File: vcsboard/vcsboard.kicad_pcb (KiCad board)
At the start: 2 copper layers, 31.5 x 33 mm, 26 parts, among them J1 Vcc / C53, J2 Video / R56, J3 Audio / C49, J4 Conn_01x06_Male, J5 Ground, Q4 2N2222A, U1 CD4053B, X2 PinHeader_1x01_P2.54mm_Vertic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, X4 PinHeader_1x01_P2.54mm_Vertic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

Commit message: add part description for more complex parts, remove unused cap
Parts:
- removed C1: 100nF, Capacitor_SMD:C_1206_3216Metric_Pad1.33x1.80mm_HandSolder
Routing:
- net Net-(C53-Pad2): track 78.9 -> 75.8 mm
- net GNDD: track 21.4 -> 19.6 mm, vias 3 -> 2

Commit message: add some more parts, use 0805 components for C53 & C54
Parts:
- C53, C54: footprint Capacitor_SMD:C_1206_3216Metric_Pad1.33x1.80mm_HandSolder -> Capacitor_SMD:C_0805_2012Metric_Pad1.18x1.45mm_HandSolder
- moved C53 0.50 mm to (118.5, 115.0)
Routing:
- net Net-(C52-Pad2): track 43.0 -> 43.7 mm

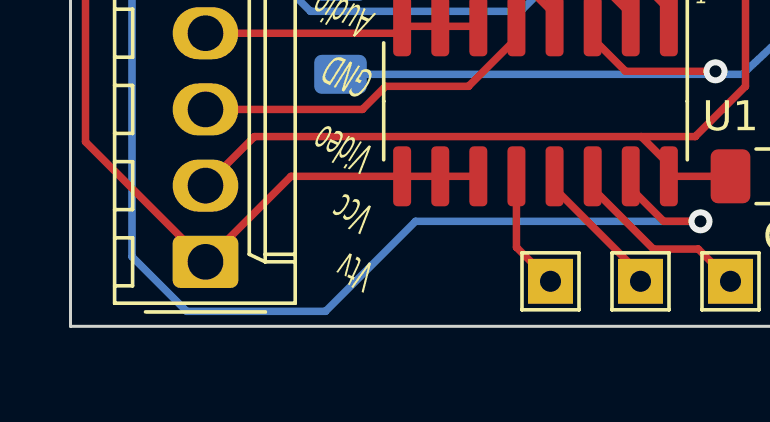
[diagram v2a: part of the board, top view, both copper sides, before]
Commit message: add star to first pin
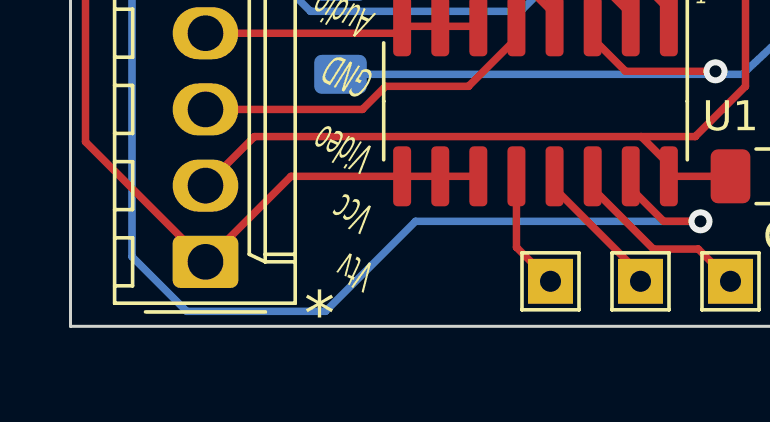
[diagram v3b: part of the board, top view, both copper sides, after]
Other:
- board text added: "*"
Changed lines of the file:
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@@
     (effects (font (size 1 0.5) (thickness 0.1) italic) (justify left))
+  )
+  (gr_text "*" (at 98.3 126.1) (layer "F.SilkS")
+    (effects (font (size 1.5 1.5) (thickness 0.3)))
   )
   (segment (start 107.405 116.5) (end 107.405 116.901751) (width 0.25) (layer "F.Cu") (net 1))

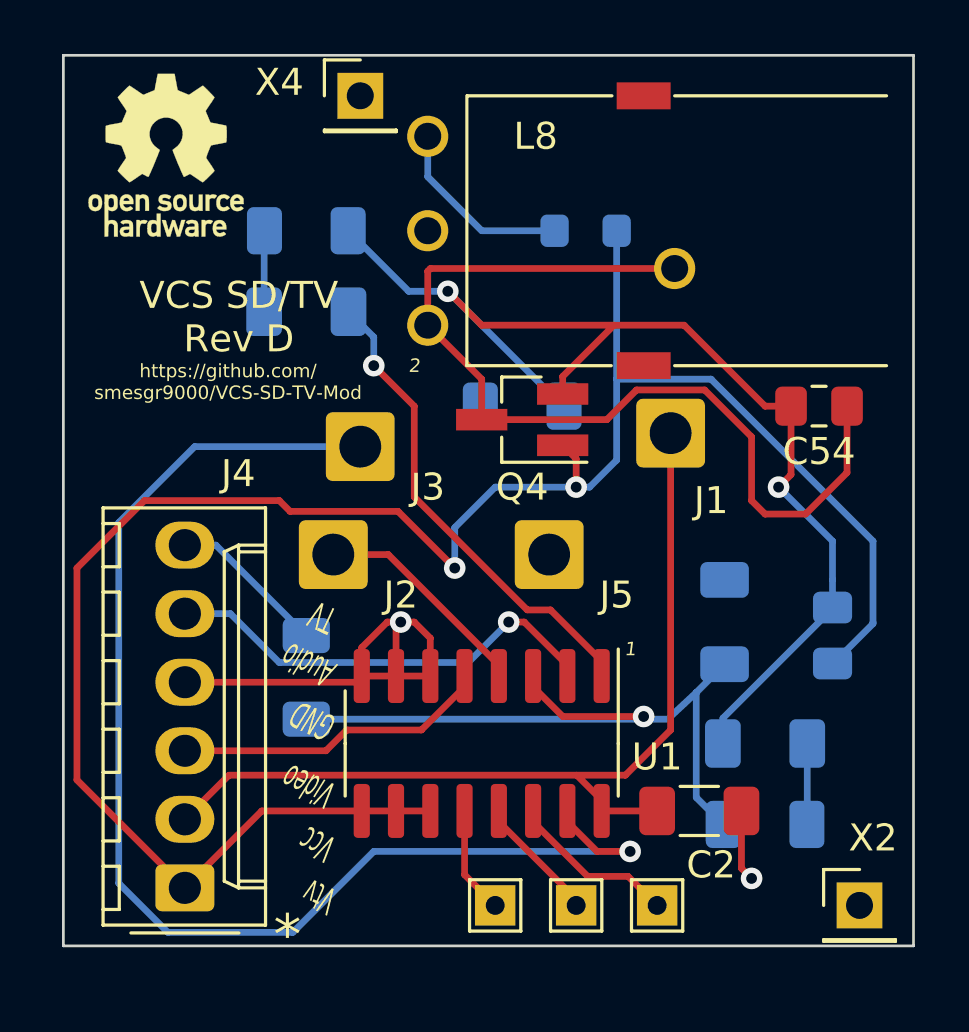
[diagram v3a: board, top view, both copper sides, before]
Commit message: update to Kicad 8
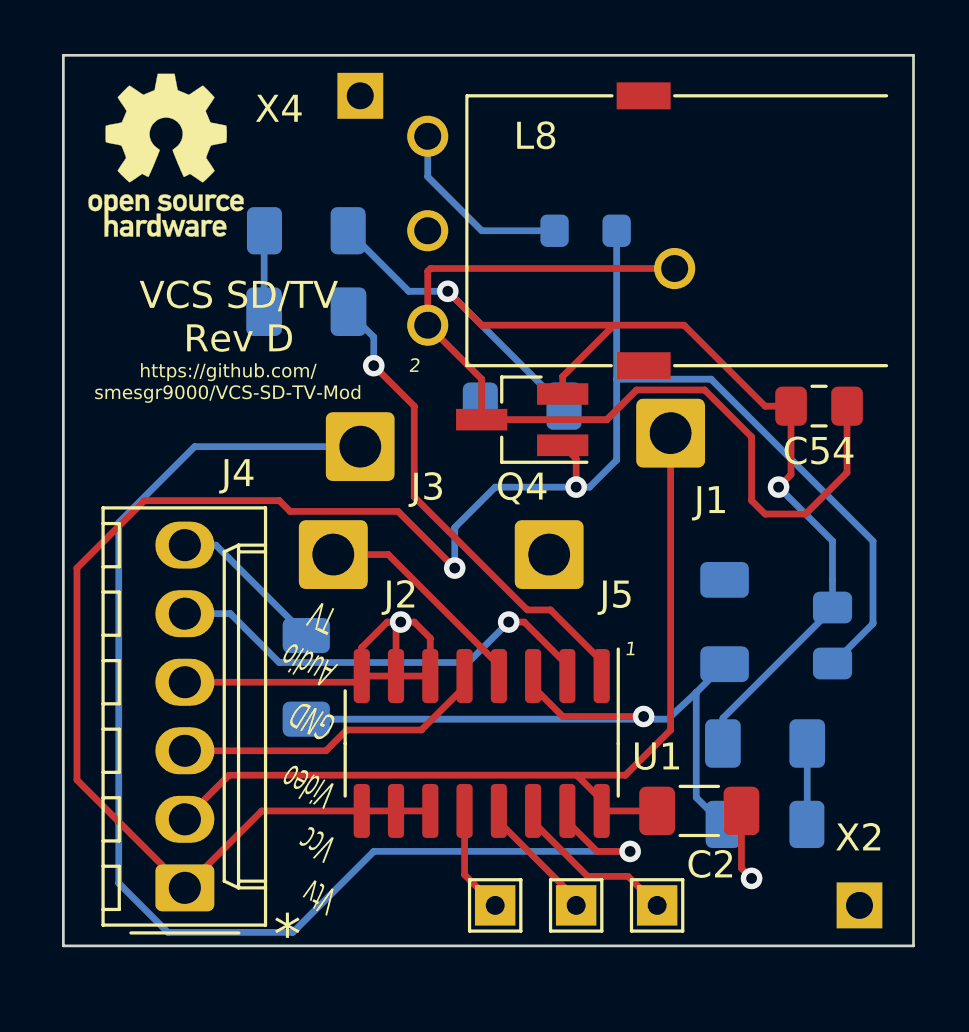
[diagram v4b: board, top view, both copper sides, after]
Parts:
- X2, X4: moved to B.Cu
- turned X2 to 180 degrees
- turned X4 to 180 degrees
